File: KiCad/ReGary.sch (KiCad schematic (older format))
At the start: 11 parts, among them J2 Conn_01x04, U4 SN74CBT16210, U5 SN74CBT16210, U6 SN74CBT16210, U7 SN74CBT16210, U8 PLCC_84_plug, U9 PLCC_84_plug

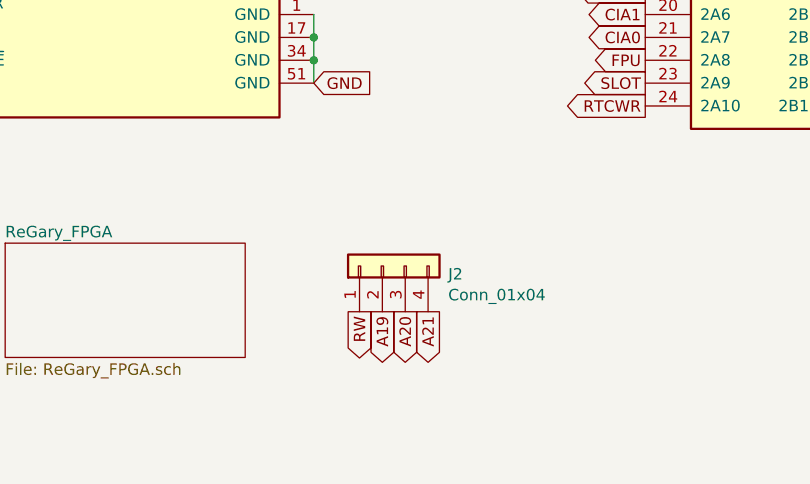
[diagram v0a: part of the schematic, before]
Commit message: Add 1.27 mm pitch pin-header for RECONFIG_N signal
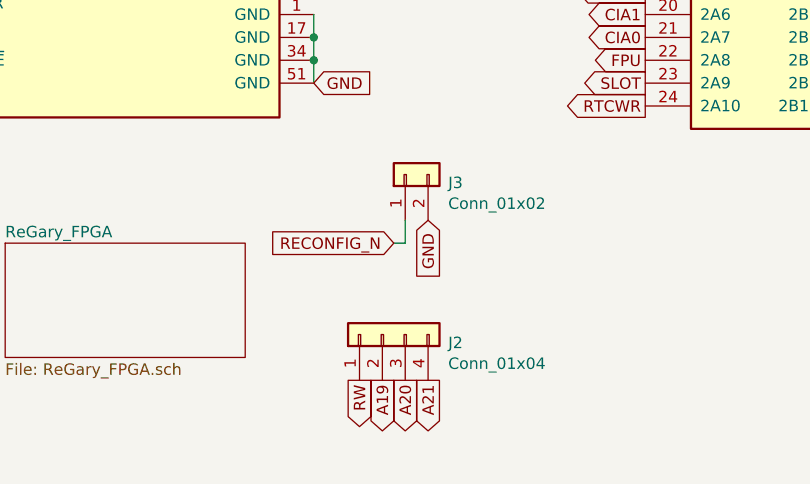
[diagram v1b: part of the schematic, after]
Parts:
- added J3: Conn_01x02, Connector_PinHeader_1.27mm:PinHeader_1x02_P1.27mm_Vertical, symbol Connector_Generic:Conn_01x02
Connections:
- net GND: now also J3.2 (Pin_2)
- new net RECONFIG_N: J3.1 (Pin_1)
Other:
- moved on the sheet: J2
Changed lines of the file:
@@
 L Connector_Generic:Conn_01x04 J2
 U 1 1 6883696B
-P 6000 6800
-F 0 "J2" V 5964 6512 50  0000 R CNN
-F 1 "Conn_01x04" V 5873 6512 50  0000 R CNN
-F 2 "Connector_PinHeader_1.27mm:PinHeader_1x04_P1.27mm_Vertical" H 6000 6800 50  0001 C CNN
-F 3 "~" H 6000 6800 50  0001 C CNN
-	1    6000 6800
+P 6000 7100
+F 0 "J2" V 5964 6812 50  0000 R CNN
+F 1 "Conn_01x04" V 5873 6812 50  0000 R CNN
+F 2 "Connector_PinHeader_1.27mm:PinHeader_1x04_P1.27mm_Vertical" H 6000 7100 50  0001 C CNN
+F 3 "~" H 6000 7100 50  0001 C CNN
+	1    6000 7100
 	0    -1   -1   0
 $EndComp
-Text GLabel 6000 7000 3    50   Output ~ 0
+Text GLabel 6000 7300 3    50   Output ~ 0
 A19
-Text GLabel 6100 7000 3    50   Output ~ 0
+Text GLabel 6100 7300 3    50   Output ~ 0
 A20
-Text GLabel 5900 7000 3    50   Output ~ 0
+Text GLabel 5900 7300 3    50   Output ~ 0
 RW
-Text GLabel 6200 7000 3    50   Output ~ 0
+Text GLabel 6200 7300 3    50   Output ~ 0
 A21
+$Comp
+L Connector_Generic:Conn_01x02 J3
+U 1 1 687BB0B9
+P 6100 6400
+F 0 "J3" V 6064 6212 50  0000 R CNN
+F 1 "Conn_01x02" V 5973 6212 50  0000 R CNN
+F 2 "Connector_PinHeader_1.27mm:PinHeader_1x02_P1.27mm_Vertical" H 6100 6400 50  0001 C CNN
+F 3 "~" H 6100 6400 50  0001 C CNN
+	1    6100 6400
+	0    -1   -1   0
+$EndComp
+Text GLabel 6200 6600 3    50   Input ~ 0
+GND
+Text GLabel 6050 6700 0    50   Input ~ 0
+RECONFIG_N
+Wire Wire Line
+	6100 6600 6100 6700
+Wire Wire Line
+	6100 6700 6050 6700
 $EndSCHEMATC
